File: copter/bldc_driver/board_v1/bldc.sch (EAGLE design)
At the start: 86 parts, among them IC1 LM339APWR, IC2 7411, IC3 7411, IC4 CD4051BPWR, IC5 FAN7388, Y1 16MHz

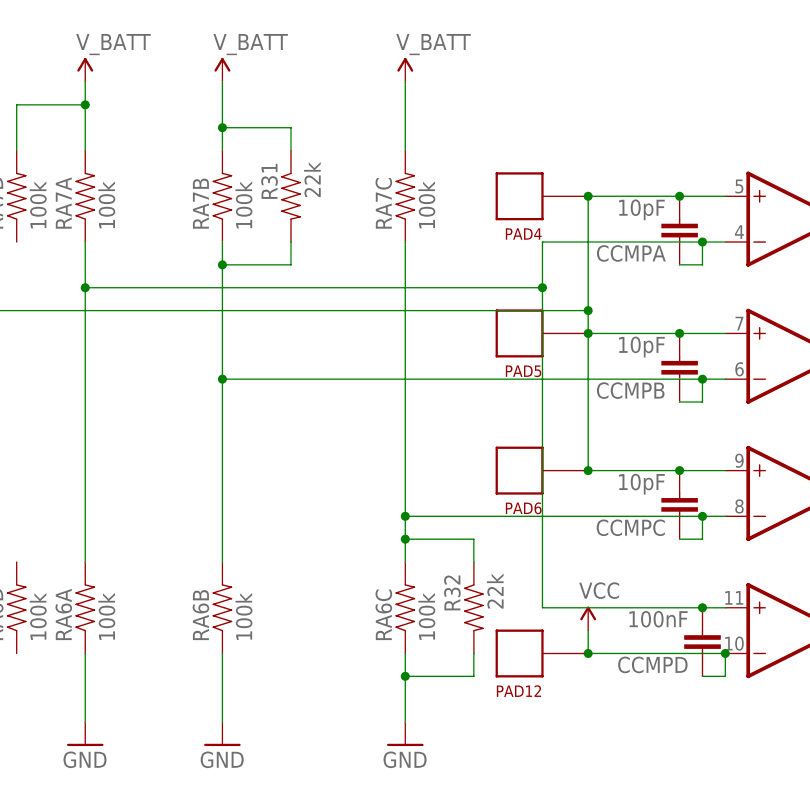
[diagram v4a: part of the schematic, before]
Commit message: got the board somewhat working, though it has trouble driving the new motors
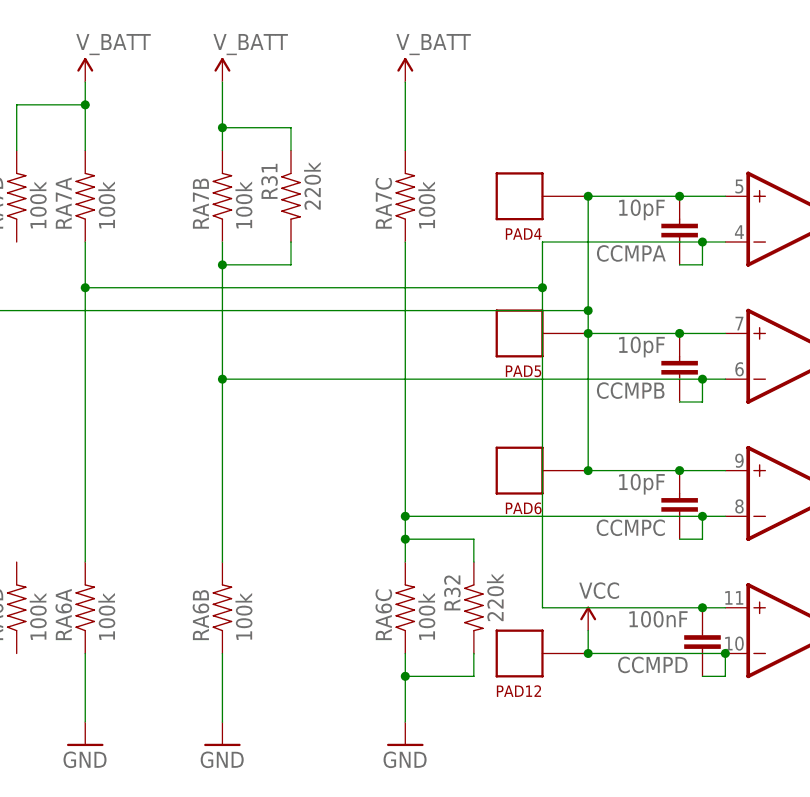
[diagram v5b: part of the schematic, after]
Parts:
- R31, R32: value 22k -> 220k
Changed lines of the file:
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@@
 <part name="SUPPLY16" library="SparkFun-Aesthetics" deviceset="V_BATT" device=""/>
 <part name="GND25" library="SparkFun-Aesthetics" deviceset="GND" device=""/>
-<part name="R31" library="SparkFun-Resistors" deviceset="RESISTOR" device="0603-RES" value="22k"/>
+<part name="R31" library="SparkFun-Resistors" deviceset="RESISTOR" device="0603-RES" value="220k"/>
 <part name="SUPPLY17" library="SparkFun-Aesthetics" deviceset="V_BATT" device=""/>
 <part name="GND26" library="SparkFun-Aesthetics" deviceset="GND" device=""/>
-<part name="R32" library="SparkFun-Resistors" deviceset="RESISTOR" device="0603-RES" value="22k"/>
+<part name="R32" library="SparkFun-Resistors" deviceset="RESISTOR" device="0603-RES" value="220k"/>
 <part name="CCMPB" library="SparkFun-Capacitors" deviceset="10NF-CER" device="" value="10pF"/>
 <part name="CCMPA" library="SparkFun-Capacitors" deviceset="10NF-CER" device="" value="10pF"/>
